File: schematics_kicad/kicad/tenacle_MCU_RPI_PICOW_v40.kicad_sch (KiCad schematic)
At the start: 3 parts, among them T201 tentacle_octobus, T202 tentacle_relay

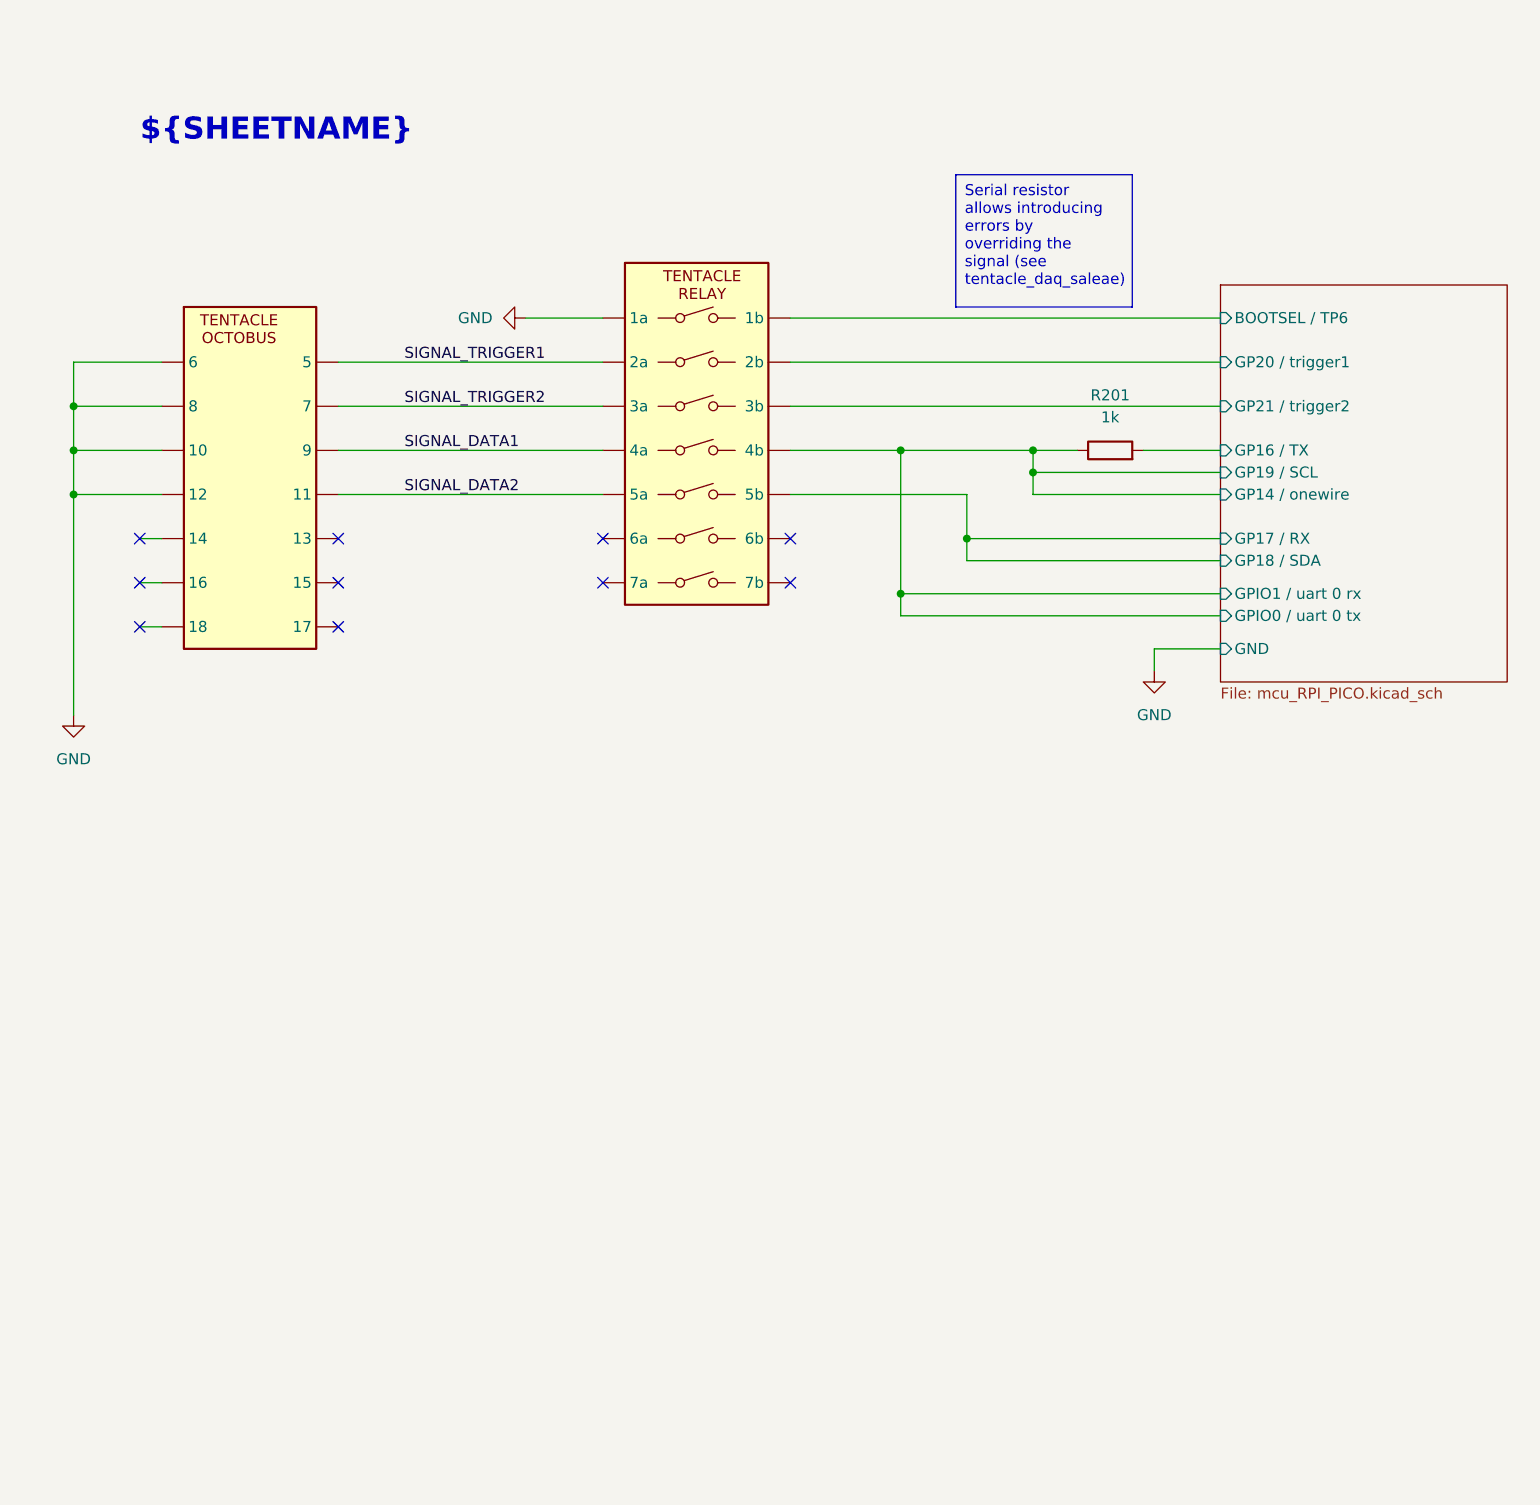
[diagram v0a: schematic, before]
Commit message: Updating schematics for RPI_PICO_W for tentacle v0.4
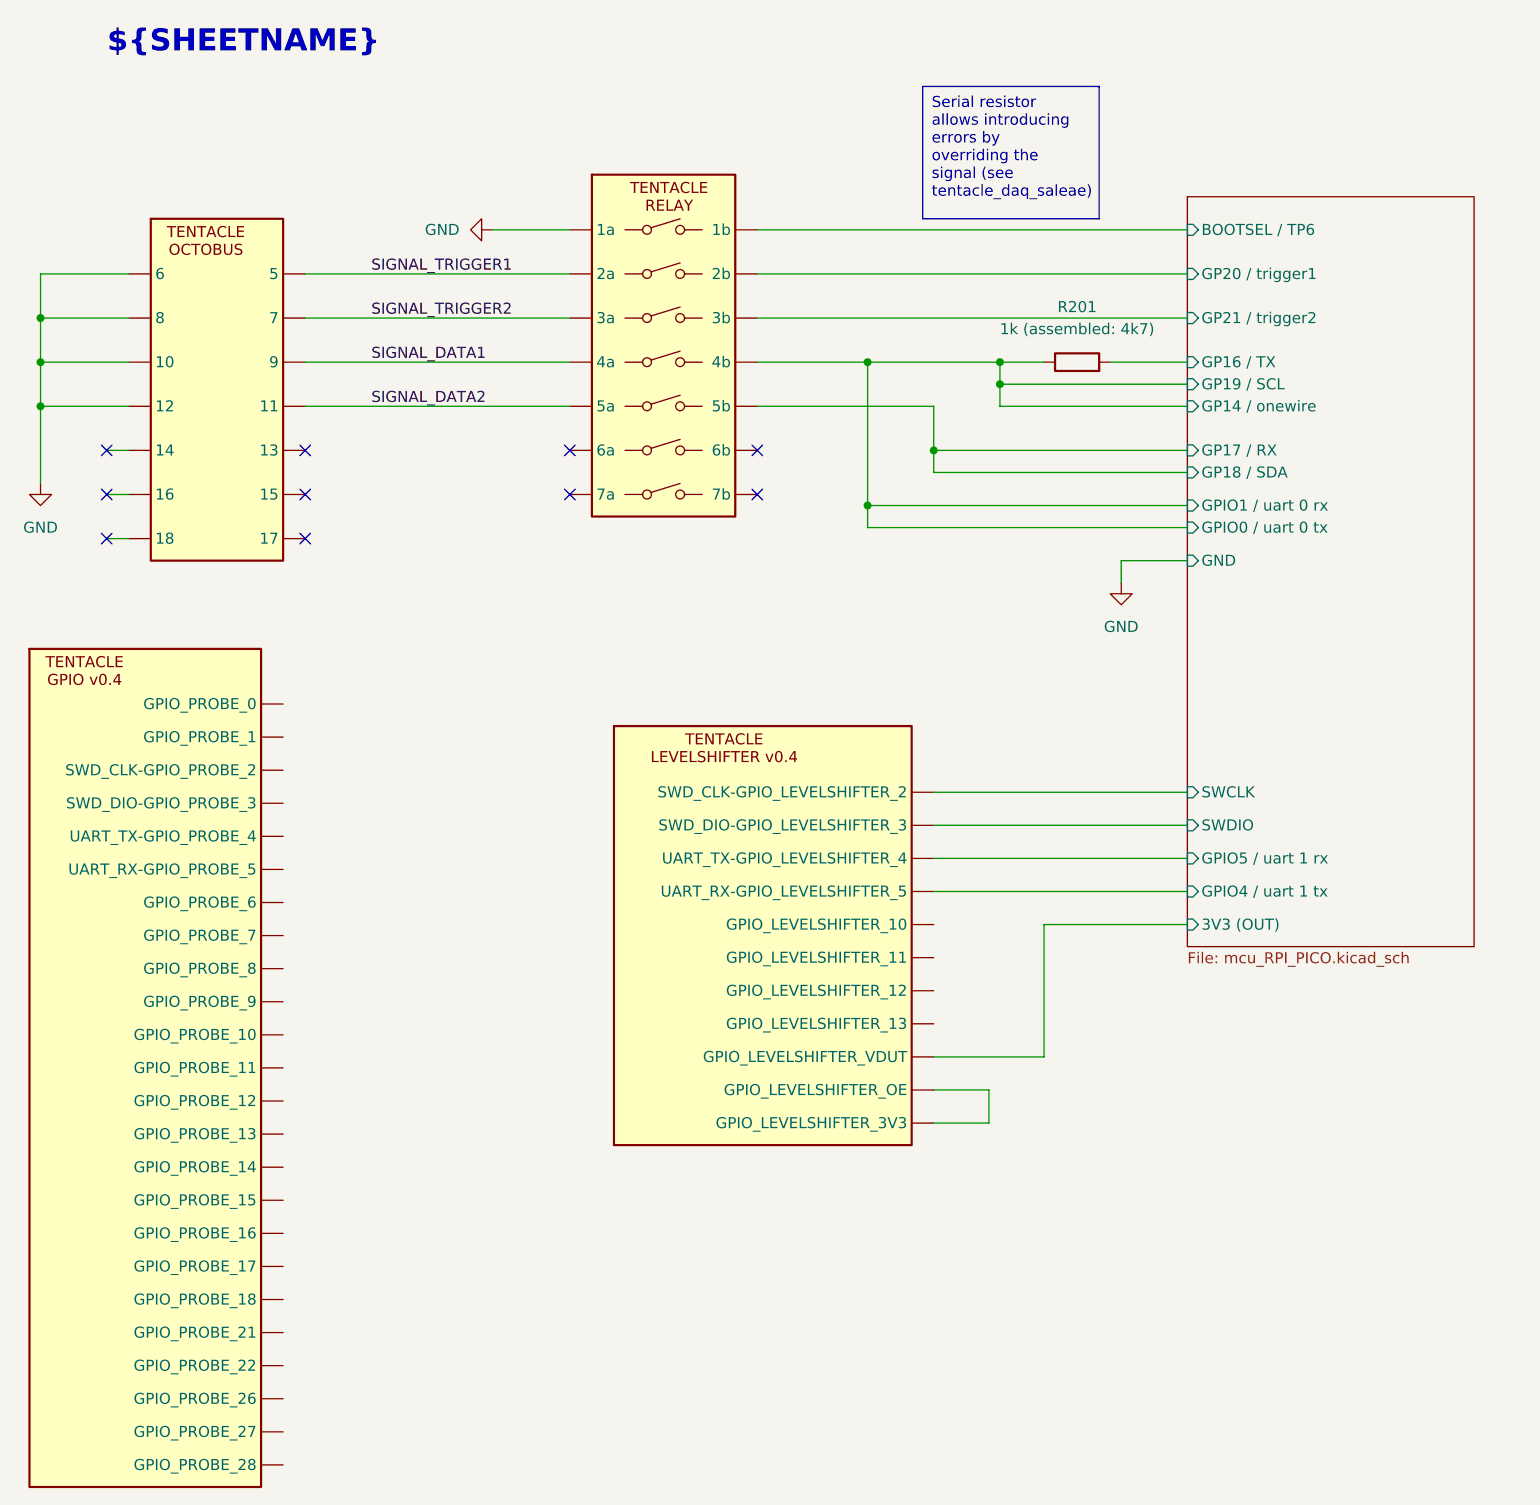
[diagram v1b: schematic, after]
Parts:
- added T1701: tentacle, symbol 00_project_library:tentacle_v04_gpio_levelshifter
- added T1702: tentacle, symbol 00_project_library:tentacle_v04_gpio_probe
- R201: value 1k -> 1k (assembled: 4k7)
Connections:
- new net MCU_RPI_PICO/3V3 (OUT): T1701. (UART_TX-GPIO_LEVELSHIFTER_4)
- new net MCU_RPI_PICO/GPIO4 / uart 1 tx: T1701. (UART_TX-GPIO_LEVELSHIFTER_4)
- new net MCU_RPI_PICO/GPIO5 / uart 1 rx: T1701. (UART_TX-GPIO_LEVELSHIFTER_4)
- new net MCU_RPI_PICO/SWCLK: T1701. (UART_TX-GPIO_LEVELSHIFTER_4)
- new net MCU_RPI_PICO/SWDIO: T1701. (UART_TX-GPIO_LEVELSHIFTER_4)
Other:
- sheet MCU_RPI_PICO ports: added 3V3 (OUT), GPIO4 / uart 1 tx, GPIO5 / uart 1 rx, SWCLK, SWDIO; removed none
- title: tentacle_MCU_RPI_PICO -> tentacle_MCU_RPI_PICOW
- moved on the sheet: R201

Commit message: tmp2
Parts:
- R201: value 1k (assembled: 4k7) -> 1k
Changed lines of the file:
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@@
 		)
 	)
-	(text_box "Serial resistor allows introducing errors by overriding the signal (see tentacle_daq_saleae)"
+	(text_box "Serial resistor allows introducing errors by overriding the signal\n(see tentacle_daq_saleae)"
 		(exclude_from_sim no)
 		(at 151.13 26.67 0)
-		(size 20.32 15.24)
+		(size 27.94 10.16)
 		(stroke
 			(width 0)
@@
 			)
 		)
-		(property "Value" "1k (assembled: 4k7)"
+		(property "Value" "1k"
 			(at 168.91 54.61 90)
 			(effects
